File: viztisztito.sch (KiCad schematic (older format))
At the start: 0 parts

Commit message: sch almost ready
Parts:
- added P1: WATER_LEVEL_CONN, symbol CONN_01X06
- added P2: BOARD_CONN, Socket_Strips:Socket_Strip_Straight_2x20, symbol CONN_02X20
- added P3: SSR&PWR, symbol CONN_01X06
- added P5: CONN_01X04, symbol CONN_01X04
- added P6: CONN_01X02, Pin_Headers:Pin_Header_Straight_1x02, symbol CONN_01X02
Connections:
- net labels added: !SSR_FAULT, +3.3V, 230VNULL, 230VPHASE, AC+, AD_CLK, AD_CS, AD_MISO, AD_MOSI, DWL0, DWL1, DWL2, DWL3, EARTH, GNDREF, MOTOR+, MOTOR-, RECT_VCC, SSR_FAULTEN, SSR_ON, T_CS, T_SCK, T_SIO
- wire segments 0 -> 49
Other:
- note added: "MEGFORDÍTOTT SORREND!"

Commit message: sch ready, begining of layout
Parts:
- added P9: CONN_01X10, libs:METZ_AST0451004, symbol CONN_01X10
- P1, P3: footprint (none) -> libs:METZ_AST1350604
- P5: footprint (none) -> libs:METZ_AST1350404
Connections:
- wire segments 49 -> 51
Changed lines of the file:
@@
 F 0 "P1" H 5350 5150 50  0000 C CNN
 F 1 "WATER_LEVEL_CONN" V 5450 4800 50  0000 C CNN
-F 2 "" H 5350 4800 60  0001 C CNN
+F 2 "libs:METZ_AST1350604" H 5350 4800 60  0001 C CNN
 F 3 "" H 5350 4800 60  0000 C CNN
 	1    5350 4800
@@
 F 0 "P3" H 6150 5150 50  0000 C CNN
 F 1 "SSR&PWR" V 6250 4800 50  0000 C CNN
-F 2 "" H 6150 4800 60  0001 C CNN
+F 2 "libs:METZ_AST1350604" H 6150 4800 60  0001 C CNN
 F 3 "" H 6150 4800 60  0000 C CNN
 	1    6150 4800
@@
 F 0 "P5" H 6800 5050 50  0000 C CNN
 F 1 "CONN_01X04" V 6900 4800 50  0000 C CNN
-F 2 "" H 6800 4800 60  0001 C CNN
+F 2 "libs:METZ_AST1350404" H 6800 4800 60  0001 C CNN
 F 3 "" H 6800 4800 60  0000 C CNN
 	1    6800 4800
@@
 Wire Wire Line
 	6100 1350 7050 1350
+$Comp
+L CONN_01X10 P9
+U 1 1 5626D6E9
+P 6550 6000
+F 0 "P9" H 6550 6550 50  0000 C CNN
+F 1 "CONN_01X10" V 6650 6000 50  0000 C CNN
+F 2 "libs:METZ_AST0451004" H 6550 6000 60  0000 C CNN
+F 3 "" H 6550 6000 60  0000 C CNN
+	1    6550 6000
+	0    1    1    0
+$EndComp
+Text GLabel 7000 5800 1    60   Input ~ 0
+RECT_VCC
+$Comp
+L GNDREF #PWR07
+U 1 1 5626F098
+P 6700 5800
+F 0 "#PWR07" H 6700 5550 50  0001 C CNN
+F 1 "GNDREF" H 6700 5650 50  0000 C CNN
+F 2 "" H 6700 5800 60  0000 C CNN
+F 3 "" H 6700 5800 60  0000 C CNN
+	1    6700 5800
+	-1   0    0    1
+$EndComp
+$Comp
+L +3.3V #PWR08
+U 1 1 5626F09E
+P 6900 5800
+F 0 "#PWR08" H 6900 5650 50  0001 C CNN
+F 1 "+3.3V" H 6900 5940 50  0000 C CNN
+F 2 "" H 6900 5800 60  0000 C CNN
+F 3 "" H 6900 5800 60  0000 C CNN
+	1    6900 5800
+	1    0    0    -1
+$EndComp
+$Comp
+L GNDREF #PWR09
+U 1 1 5626F0A4
+P 6800 5800
+F 0 "#PWR09" H 6800 5550 50  0001 C CNN
+F 1 "GNDREF" H 6800 5650 50  0000 C CNN
+F 2 "" H 6800 5800 60  0000 C CNN
+F 3 "" H 6800 5800 60  0000 C CNN
+	1    6800 5800
+	-1   0    0    1
+$EndComp
+Text GLabel 6500 5800 1    60   Input ~ 0
+EARTH
+Text GLabel 6100 5800 1    60   Input ~ 0
+MOTOR+
+Text GLabel 6300 5000 0    60   Input ~ 0
+MOTOR-
+Text GLabel 6200 5800 1    60   Input ~ 0
+EARTH
+Wire Wire Line
+	6300 5000 6300 5800
+Wire Wire Line
+	6300 5800 6400 5800
+Text GLabel 6600 5800 1    60   Input ~ 0
+230VPHASE
+Text GLabel 6300 5000 2    60   Input ~ 0
+230VNULL
 $EndSCHEMATC

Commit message: layout beginning
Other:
- moved on the sheet: P9
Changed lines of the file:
@@
 L CONN_01X10 P9
 U 1 1 5626D6E9
-P 6550 6000
-F 0 "P9" H 6550 6550 50  0000 C CNN
-F 1 "CONN_01X10" V 6650 6000 50  0000 C CNN
-F 2 "libs:METZ_AST0451004" H 6550 6000 60  0000 C CNN
-F 3 "" H 6550 6000 60  0000 C CNN
-	1    6550 6000
+P 6550 6250
+F 0 "P9" H 6550 6800 50  0000 C CNN
+F 1 "CONN_01X10" V 6650 6250 50  0000 C CNN
+F 2 "libs:METZ_AST0451004" H 6550 6250 60  0000 C CNN
+F 3 "" H 6550 6250 60  0000 C CNN
+	1    6550 6250
 	0    1    1    0
 $EndComp
-Text GLabel 7000 5800 1    60   Input ~ 0
+Text GLabel 6400 6050 1    60   Input ~ 0
 RECT_VCC
 $Comp
 L GNDREF #PWR07
 U 1 1 5626F098
-P 6700 5800
-F 0 "#PWR07" H 6700 5550 50  0001 C CNN
-F 1 "GNDREF" H 6700 5650 50  0000 C CNN
-F 2 "" H 6700 5800 60  0000 C CNN
-F 3 "" H 6700 5800 60  0000 C CNN
-	1    6700 5800
+P 6100 6050
+F 0 "#PWR07" H 6100 5800 50  0001 C CNN
+F 1 "GNDREF" H 6100 5900 50  0000 C CNN
+F 2 "" H 6100 6050 60  0000 C CNN
+F 3 "" H 6100 6050 60  0000 C CNN
+	1    6100 6050
 	-1   0    0    1
 $EndComp
@@
 L +3.3V #PWR08
 U 1 1 5626F09E
-P 6900 5800
-F 0 "#PWR08" H 6900 5650 50  0001 C CNN
-F 1 "+3.3V" H 6900 5940 50  0000 C CNN
-F 2 "" H 6900 5800 60  0000 C CNN
-F 3 "" H 6900 5800 60  0000 C CNN
-	1    6900 5800
+P 6300 6050
+F 0 "#PWR08" H 6300 5900 50  0001 C CNN
+F 1 "+3.3V" H 6300 6190 50  0000 C CNN
+F 2 "" H 6300 6050 60  0000 C CNN
+F 3 "" H 6300 6050 60  0000 C CNN
+	1    6300 6050
 	1    0    0    -1
 $EndComp
@@
 L GNDREF #PWR09
 U 1 1 5626F0A4
-P 6800 5800
-F 0 "#PWR09" H 6800 5550 50  0001 C CNN
-F 1 "GNDREF" H 6800 5650 50  0000 C CNN
-F 2 "" H 6800 5800 60  0000 C CNN
-F 3 "" H 6800 5800 60  0000 C CNN
-	1    6800 5800
+P 6200 6050
+F 0 "#PWR09" H 6200 5800 50  0001 C CNN
+F 1 "GNDREF" H 6200 5900 50  0000 C CNN
+F 2 "" H 6200 6050 60  0000 C CNN
+F 3 "" H 6200 6050 60  0000 C CNN
+	1    6200 6050
 	-1   0    0    1
 $EndComp
-Text GLabel 6500 5800 1    60   Input ~ 0
+Text GLabel 6900 6050 1    60   Input ~ 0
 EARTH
-Text GLabel 6100 5800 1    60   Input ~ 0
+Text GLabel 6500 6050 1    60   Input ~ 0
 MOTOR+
-Text GLabel 6300 5000 0    60   Input ~ 0
+Text GLabel 6700 5250 0    60   Input ~ 0
 MOTOR-
-Text GLabel 6200 5800 1    60   Input ~ 0
+Text GLabel 6600 6050 1    60   Input ~ 0
 EARTH
 Wire Wire Line
-	6300 5000 6300 5800
+	6700 5250 6700 6050
 Wire Wire Line
-	6300 5800 6400 5800
-Text GLabel 6600 5800 1    60   Input ~ 0
+	6700 6050 6800 6050
+Text GLabel 7000 6050 1    60   Input ~ 0
 230VPHASE
-Text GLabel 6300 5000 2    60   Input ~ 0
+Text GLabel 6700 5250 2    60   Input ~ 0
 230VNULL
 $EndSCHEMATC

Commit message: maybe final
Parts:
- added P10, P11, P12, P13: CONN_01X01, Mounting_Holes:MountingHole_4-5mm, symbol CONN_01X01
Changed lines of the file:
@@
 	7900 5100 7900 5400
 Wire Wire Line
-	7900 4600 7900 4250
-Wire Wire Line
 	8000 4600 8000 4250
 Wire Wire Line
@@
 	8600 4600 8600 4250
 Wire Wire Line
-	8800 4600 8800 4250
-Wire Wire Line
 	8900 4600 8900 4250
 Wire Wire Line
 	9000 4600 9000 4250
-Wire Wire Line
-	9100 4600 9100 4250
 Wire Wire Line
 	9200 4600 9200 4250
@@
 Text Label 8250 1850 0    60   ~ 0
 AD_CLK
-Text Label 7900 4250 1    60   ~ 0
+Text Label 8000 4250 1    60   ~ 0
 DWL0
-Text Label 8000 4250 1    60   ~ 0
+Text Label 8100 4250 1    60   ~ 0
 DWL1
-Text Label 8100 4250 1    60   ~ 0
+Text Label 8200 4250 1    60   ~ 0
 DWL2
-Text Label 8200 4250 1    60   ~ 0
+Text Label 8300 4250 1    60   ~ 0
 DWL3
-Text Label 8300 4250 1    60   ~ 0
+Text Label 9500 4250 1    60   ~ 0
 !SSR_FAULT
+Text Label 9400 4250 1    60   ~ 0
+SSR_FAULTEN
+Text Label 9300 4250 1    60   ~ 0
+SSR_ON
 Text Label 8500 4250 1    60   ~ 0
-SSR_FAULTEN
+T_SCK
 Text Label 8600 4250 1    60   ~ 0
-SSR_ON
-Text Label 8800 4250 1    60   ~ 0
-T_SCK
+T_SIO
+Text Label 8400 4250 1    60   ~ 0
+T_CS
+Text Label 9200 4250 1    60   ~ 0
+AD_CS
+Text Label 9000 4250 1    60   ~ 0
+AD_MOSI
 Text Label 8900 4250 1    60   ~ 0
-T_SIO
-Text Label 9000 4250 1    60   ~ 0
-T_CS
-Text Label 9100 4250 1    60   ~ 0
-AD_CS
-Text Label 9200 4250 1    60   ~ 0
-AD_MOSI
-Text Label 9300 4250 1    60   ~ 0
 AD_MISO
-Text Label 9400 4250 1    60   ~ 0
+Text Label 8700 4250 1    60   ~ 0
 AD_CLK
 Text Notes 9900 4900 0    60   ~ 0
@@
 	1    0    0    -1
 $EndComp
+Text GLabel 6900 6050 1    60   Input ~ 0
+EARTH
+Text GLabel 6500 6050 1    60   Input ~ 0
+MOTOR+
+Text GLabel 6700 5250 0    60   Input ~ 0
+MOTOR-
+Text GLabel 6600 6050 1    60   Input ~ 0
+EARTH
+Wire Wire Line
+	6700 5250 6700 6050
+Wire Wire Line
+	6700 6050 6800 6050
+Text GLabel 7000 6050 1    60   Input ~ 0
+230VPHASE
+Text GLabel 6700 5250 2    60   Input ~ 0
+230VNULL
+$Comp
+L CONN_01X01 P12
+U 1 1 562A651D
+P 3800 5400
+F 0 "P12" H 3800 5500 50  0000 C CNN
+F 1 "CONN_01X01" V 3900 5400 50  0000 C CNN
+F 2 "Mounting_Holes:MountingHole_4-5mm" H 3800 5400 60  0001 C CNN
+F 3 "" H 3800 5400 60  0000 C CNN
+	1    3800 5400
+	1    0    0    -1
+$EndComp
+$Comp
+L CONN_01X01 P11
+U 1 1 562A65E7
+P 3800 5050
+F 0 "P11" H 3800 5150 50  0000 C CNN
+F 1 "CONN_01X01" V 3900 5050 50  0000 C CNN
+F 2 "Mounting_Holes:MountingHole_4-5mm" H 3800 5050 60  0001 C CNN
+F 3 "" H 3800 5050 60  0000 C CNN
+	1    3800 5050
+	1    0    0    -1
+$EndComp
+$Comp
+L CONN_01X01 P10
+U 1 1 562A66C7
+P 3800 4700
+F 0 "P10" H 3800 4800 50  0000 C CNN
+F 1 "CONN_01X01" V 3900 4700 50  0000 C CNN
+F 2 "Mounting_Holes:MountingHole_4-5mm" H 3800 4700 60  0001 C CNN
+F 3 "" H 3800 4700 60  0000 C CNN
+	1    3800 4700
+	1    0    0    -1
+$EndComp
+$Comp
+L CONN_01X01 P13
+U 1 1 562A67A4
+P 3800 5750
+F 0 "P13" H 3800 5850 50  0000 C CNN
+F 1 "CONN_01X01" V 3900 5750 50  0000 C CNN
+F 2 "Mounting_Holes:MountingHole_4-5mm" H 3800 5750 60  0001 C CNN
+F 3 "" H 3800 5750 60  0000 C CNN
+	1    3800 5750
+	1    0    0    -1
+$EndComp
+Wire Wire Line
+	9600 4600 9600 4250
+Wire Wire Line
+	8700 4600 8700 4250
+Wire Wire Line
+	8400 4600 8400 4250
 $Comp
 L GNDREF #PWR09
@@
 	-1   0    0    1
 $EndComp
-Text GLabel 6900 6050 1    60   Input ~ 0
-EARTH
-Text GLabel 6500 6050 1    60   Input ~ 0
-MOTOR+
-Text GLabel 6700 5250 0    60   Input ~ 0
-MOTOR-
-Text GLabel 6600 6050 1    60   Input ~ 0
-EARTH
-Wire Wire Line
-	6700 5250 6700 6050
-Wire Wire Line
-	6700 6050 6800 6050
-Text GLabel 7000 6050 1    60   Input ~ 0
-230VPHASE
-Text GLabel 6700 5250 2    60   Input ~ 0
-230VNULL
 $EndSCHEMATC

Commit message: almost final...
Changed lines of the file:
@@
 F6 "CURR_SENSE_DIRECT" I R 6100 1150 60
 F7 "CURR_SENSE_FILTERED" I R 6100 1050 60
-F8 "CURR_SENSE_FILTERED_2" I R 6100 1250 60
-F9 "CURR_SENSE_DIRECT_2" I R 6100 1350 60
+F8 "CURR_SENSE_FILTERED_2" I R 6100 1350 60
+F9 "CURR_SENSE_DIRECT_2" I R 6100 1250 60
 $EndSheet
 $Sheet

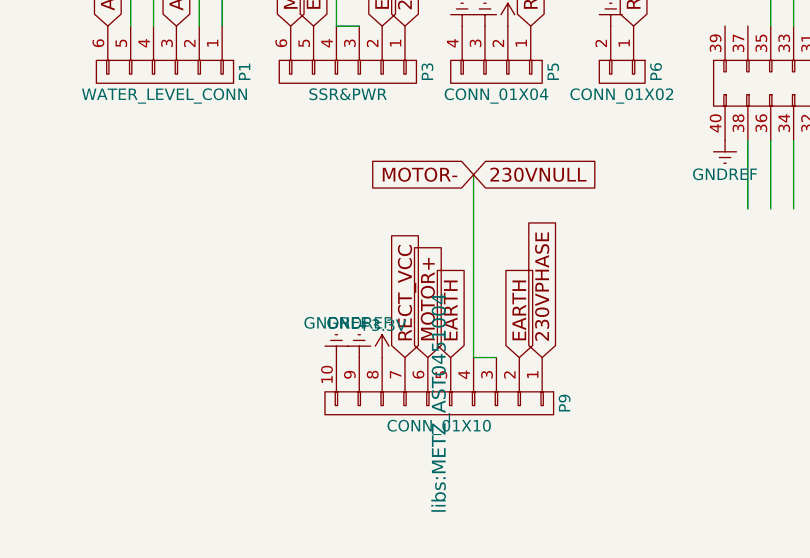
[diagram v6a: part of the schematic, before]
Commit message: new layout, added psu
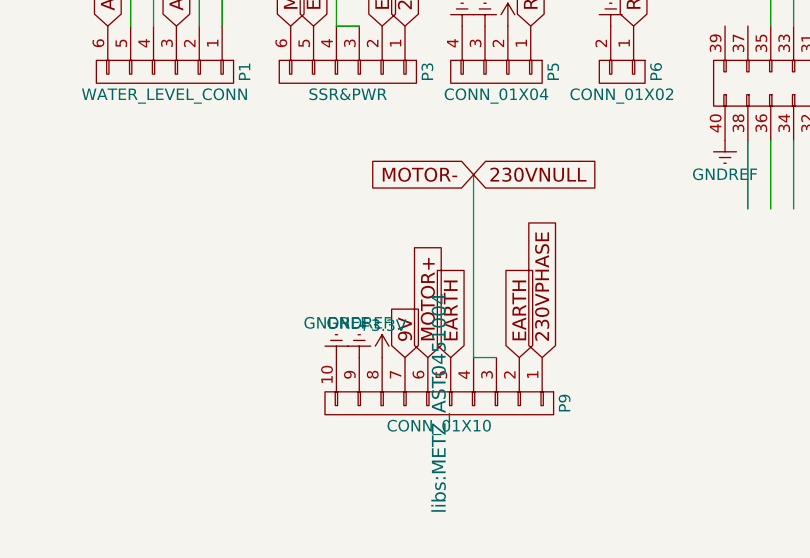
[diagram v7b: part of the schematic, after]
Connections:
- net labels added: 9V
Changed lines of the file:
@@
 LIBS:contrib
 LIBS:valves
-LIBS:mylib
+LIBS:analog_devices
+LIBS:libs
 LIBS:viztisztito-cache
 EELAYER 25 0
@@
 	0    1    1    0
 $EndComp
-Text GLabel 6400 6050 1    60   Input ~ 0
-RECT_VCC
 $Comp
 L GNDREF #PWR07
@@
 	-1   0    0    1
 $EndComp
+Text GLabel 6400 6050 1    60   Input ~ 0
+9V
 $EndSCHEMATC

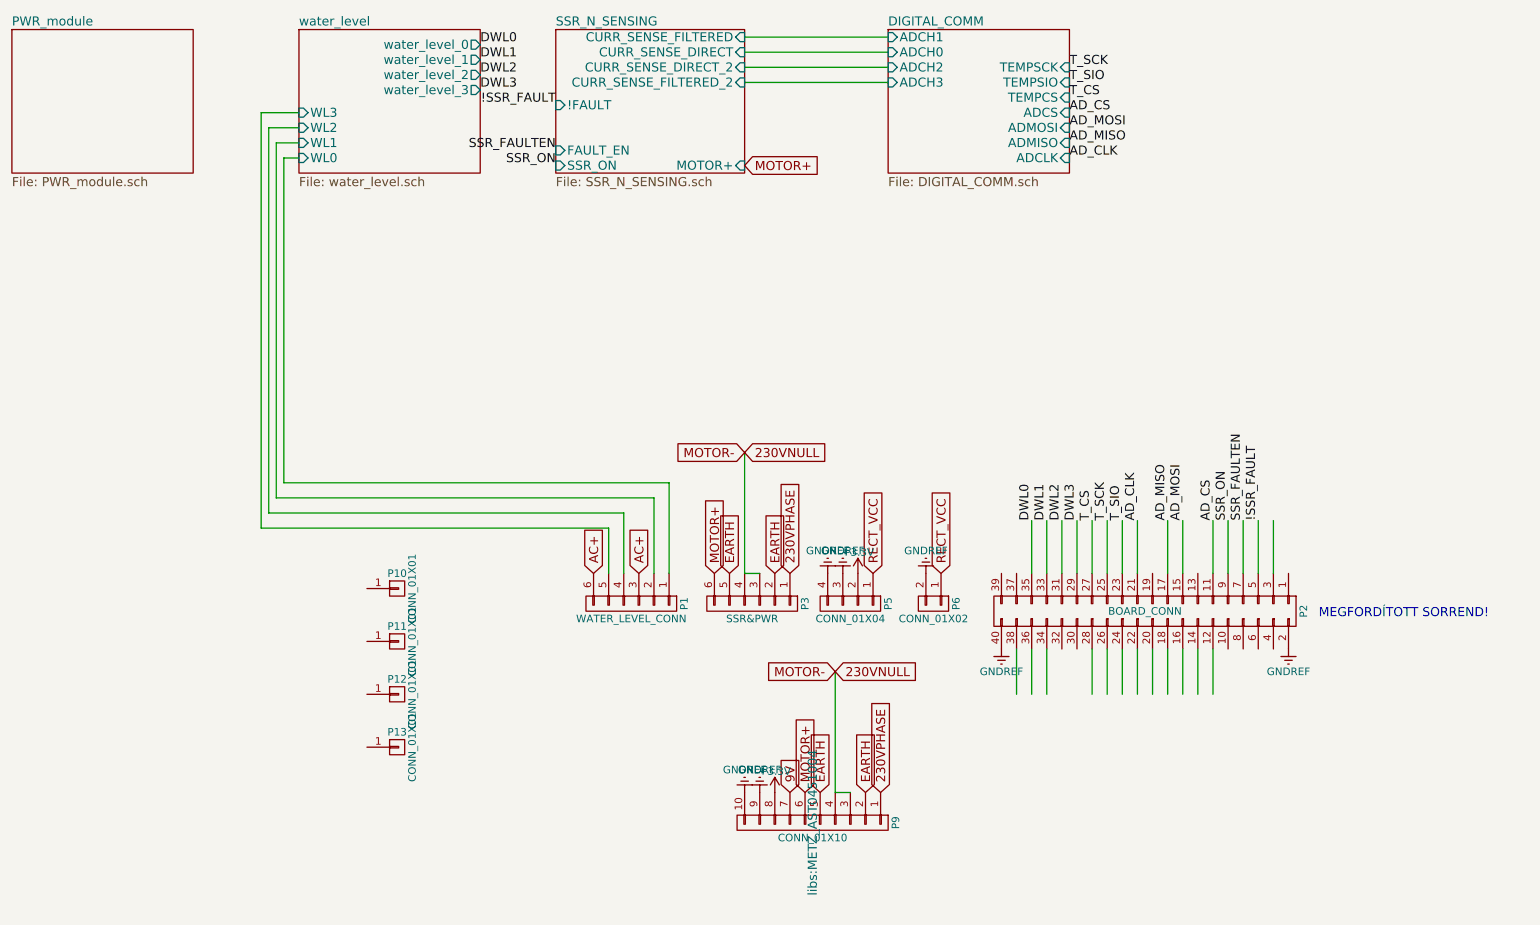
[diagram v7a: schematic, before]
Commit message: - this version has a new power supply 5V 15W - new water level sensing using protectbt
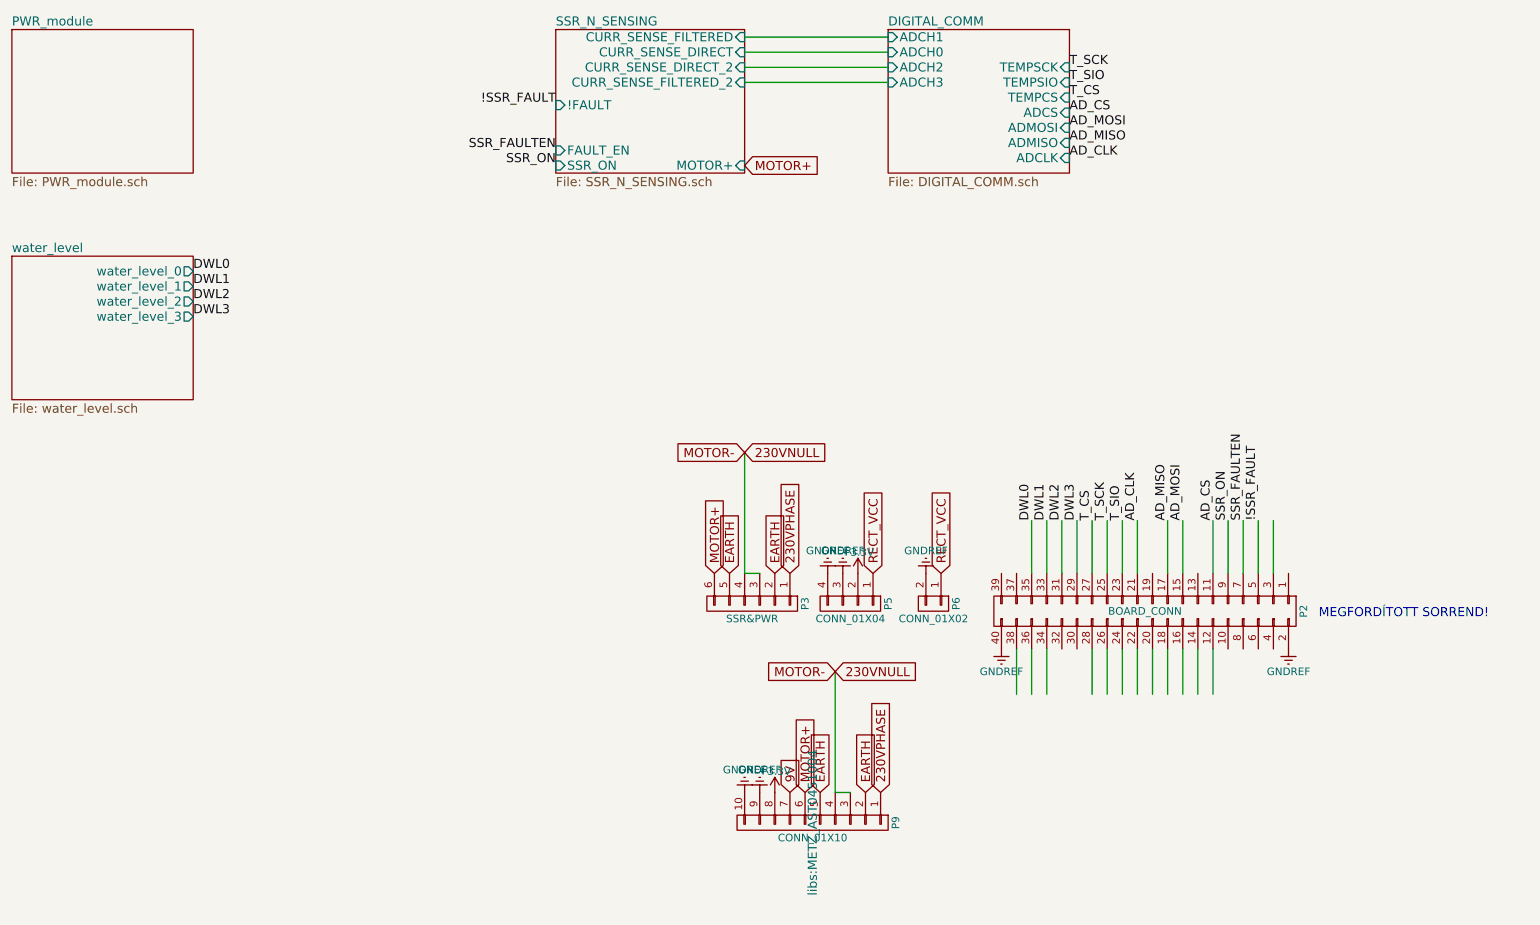
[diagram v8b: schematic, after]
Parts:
- removed P1: WATER_LEVEL_CONN, libs:METZ_AST1350604, symbol CONN_01X06
- removed P10, P11, P12, P13: CONN_01X01, Mounting_Holes:MountingHole_4-5mm, symbol CONN_01X01
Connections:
- net labels removed: AC+
- wire segments 51 -> 35
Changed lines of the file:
@@
 LIBS:valves
 LIBS:analog_devices
-LIBS:libs
+LIBS:vtx-214-015-112
 LIBS:viztisztito-cache
 EELAYER 25 0
@@
 $EndSheet
 $Sheet
-S 3150 1000 1200 950
+S 1250 2500 1200 950
 U 5614D8B0
 F0 "water_level" 60
 F1 "water_level.sch" 60
-F2 "water_level_0" O R 4350 1100 60
-F3 "water_level_1" O R 4350 1200 60
-F4 "water_level_2" O R 4350 1300 60
-F5 "water_level_3" O R 4350 1400 60
-F6 "WL1" I L 3150 1750 60
-F7 "WL2" I L 3150 1650 60
-F8 "WL3" I L 3150 1550 60
-F9 "WL0" I L 3150 1850 60
+F2 "water_level_0" O R 2450 2600 60
+F3 "water_level_1" O R 2450 2700 60
+F4 "water_level_2" O R 2450 2800 60
+F5 "water_level_3" O R 2450 2900 60
 $EndSheet
 $Sheet
@@
 $EndSheet
 $Comp
-L CONN_01X06 P1
-U 1 1 561BBFA0
-P 5350 4800
-F 0 "P1" H 5350 5150 50  0000 C CNN
-F 1 "WATER_LEVEL_CONN" V 5450 4800 50  0000 C CNN
-F 2 "libs:METZ_AST1350604" H 5350 4800 60  0001 C CNN
-F 3 "" H 5350 4800 60  0000 C CNN
-	1    5350 4800
-	0    1    1    0
-$EndComp
-$Comp
 L CONN_01X06 P3
 U 1 1 561BC3B1
@@
 	-1   0    0    1
 $EndComp
-Text GLabel 5400 4600 1    60   Input ~ 0
-AC+
-Text GLabel 5100 4600 1    60   Input ~ 0
-AC+
 $Comp
 L GNDREF #PWR05
@@
 	6100 4600 6200 4600
 Wire Wire Line
-	3150 1850 3050 1850
-Wire Wire Line
-	3050 1850 3050 4000
-Wire Wire Line
-	3050 4000 5600 4000
-Wire Wire Line
-	5600 4000 5600 4600
-Wire Wire Line
-	3150 1750 3000 1750
-Wire Wire Line
-	3000 1750 3000 4100
-Wire Wire Line
-	3000 4100 5500 4100
-Wire Wire Line
-	5500 4100 5500 4600
-Wire Wire Line
-	3150 1650 2950 1650
-Wire Wire Line
-	2950 1650 2950 4200
-Wire Wire Line
-	2950 4200 5300 4200
-Wire Wire Line
-	5300 4200 5300 4600
-Wire Wire Line
-	5200 4600 5200 4300
-Wire Wire Line
-	5200 4300 2900 4300
-Wire Wire Line
-	2900 4300 2900 1550
-Wire Wire Line
-	2900 1550 3150 1550
-Wire Wire Line
 	9200 5100 9200 5400
 Wire Wire Line
@@
 Text Label 4850 1500 2    60   ~ 0
 !SSR_FAULT
-Text Label 4350 1100 0    60   ~ 0
+Text Label 2450 2600 0    60   ~ 0
 DWL0
-Text Label 4350 1200 0    60   ~ 0
+Text Label 2450 2700 0    60   ~ 0
 DWL1
-Text Label 4350 1300 0    60   ~ 0
+Text Label 2450 2800 0    60   ~ 0
 DWL2
-Text Label 4350 1400 0    60   ~ 0
+Text Label 2450 2900 0    60   ~ 0
 DWL3
 Text Label 4850 1900 2    60   ~ 0
@@
 Text GLabel 6700 5250 2    60   Input ~ 0
 230VNULL
-$Comp
-L CONN_01X01 P12
-U 1 1 562A651D
-P 3800 5400
-F 0 "P12" H 3800 5500 50  0000 C CNN
-F 1 "CONN_01X01" V 3900 5400 50  0000 C CNN
-F 2 "Mounting_Holes:MountingHole_4-5mm" H 3800 5400 60  0001 C CNN
-F 3 "" H 3800 5400 60  0000 C CNN
-	1    3800 5400
-	1    0    0    -1
-$EndComp
-$Comp
-L CONN_01X01 P11
-U 1 1 562A65E7
-P 3800 5050
-F 0 "P11" H 3800 5150 50  0000 C CNN
-F 1 "CONN_01X01" V 3900 5050 50  0000 C CNN
-F 2 "Mounting_Holes:MountingHole_4-5mm" H 3800 5050 60  0001 C CNN
-F 3 "" H 3800 5050 60  0000 C CNN
-	1    3800 5050
-	1    0    0    -1
-$EndComp
-$Comp
-L CONN_01X01 P10
-U 1 1 562A66C7
-P 3800 4700
-F 0 "P10" H 3800 4800 50  0000 C CNN
-F 1 "CONN_01X01" V 3900 4700 50  0000 C CNN
-F 2 "Mounting_Holes:MountingHole_4-5mm" H 3800 4700 60  0001 C CNN
-F 3 "" H 3800 4700 60  0000 C CNN
-	1    3800 4700
-	1    0    0    -1
-$EndComp
-$Comp
-L CONN_01X01 P13
-U 1 1 562A67A4
-P 3800 5750
-F 0 "P13" H 3800 5850 50  0000 C CNN
-F 1 "CONN_01X01" V 3900 5750 50  0000 C CNN
-F 2 "Mounting_Holes:MountingHole_4-5mm" H 3800 5750 60  0001 C CNN
-F 3 "" H 3800 5750 60  0000 C CNN
-	1    3800 5750
-	1    0    0    -1
-$EndComp
 Wire Wire Line
 	9600 4600 9600 4250
